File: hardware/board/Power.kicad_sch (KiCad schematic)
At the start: 40 parts

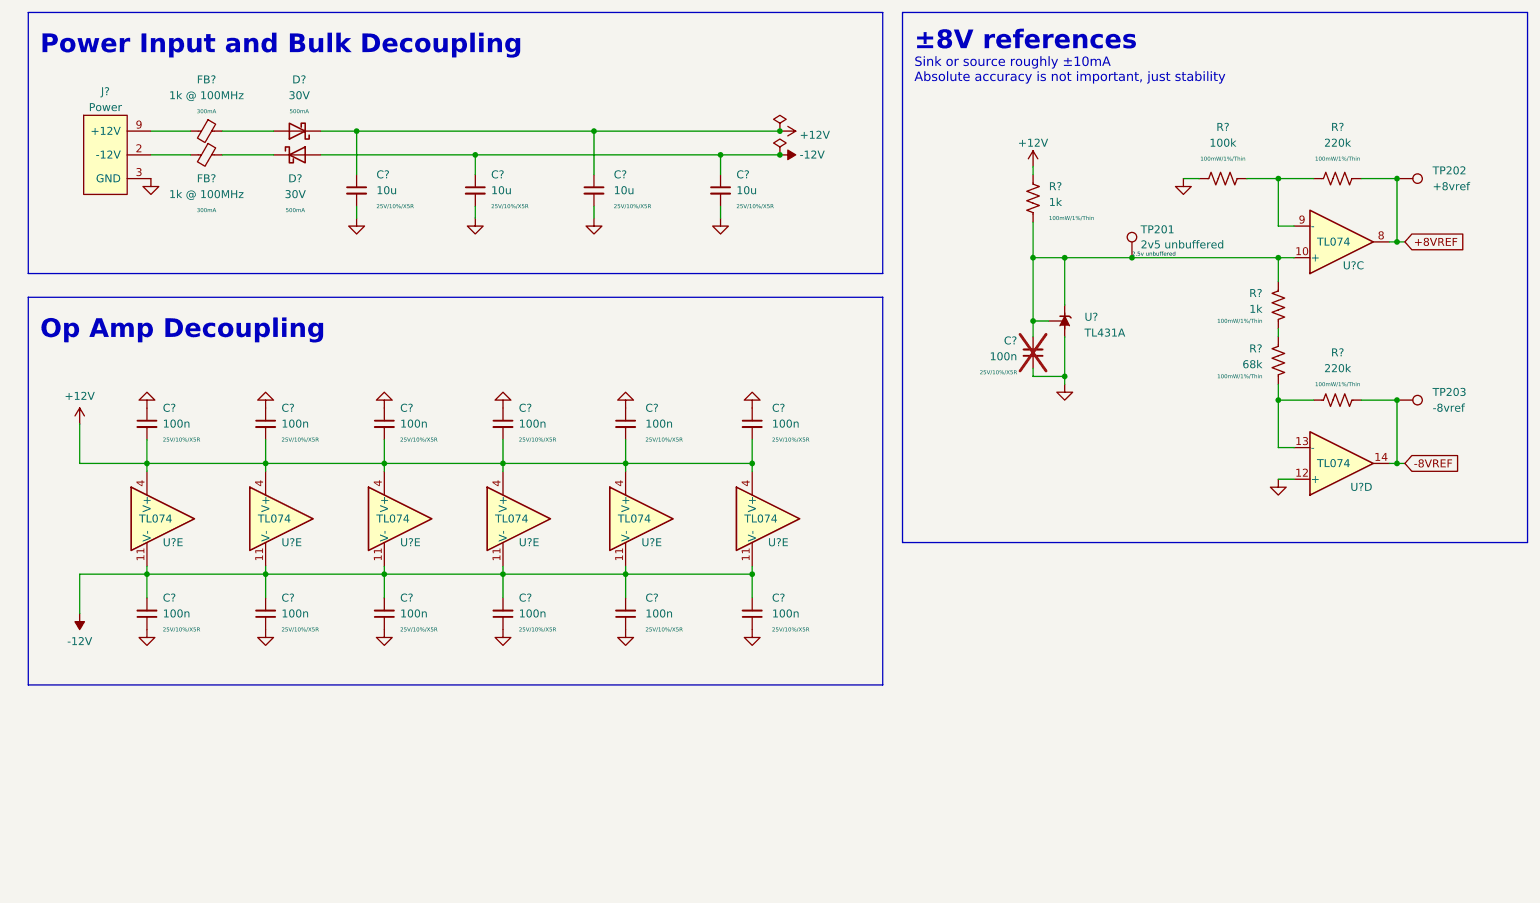
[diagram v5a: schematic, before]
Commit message: hardware: use new Winterbloom sheet layout
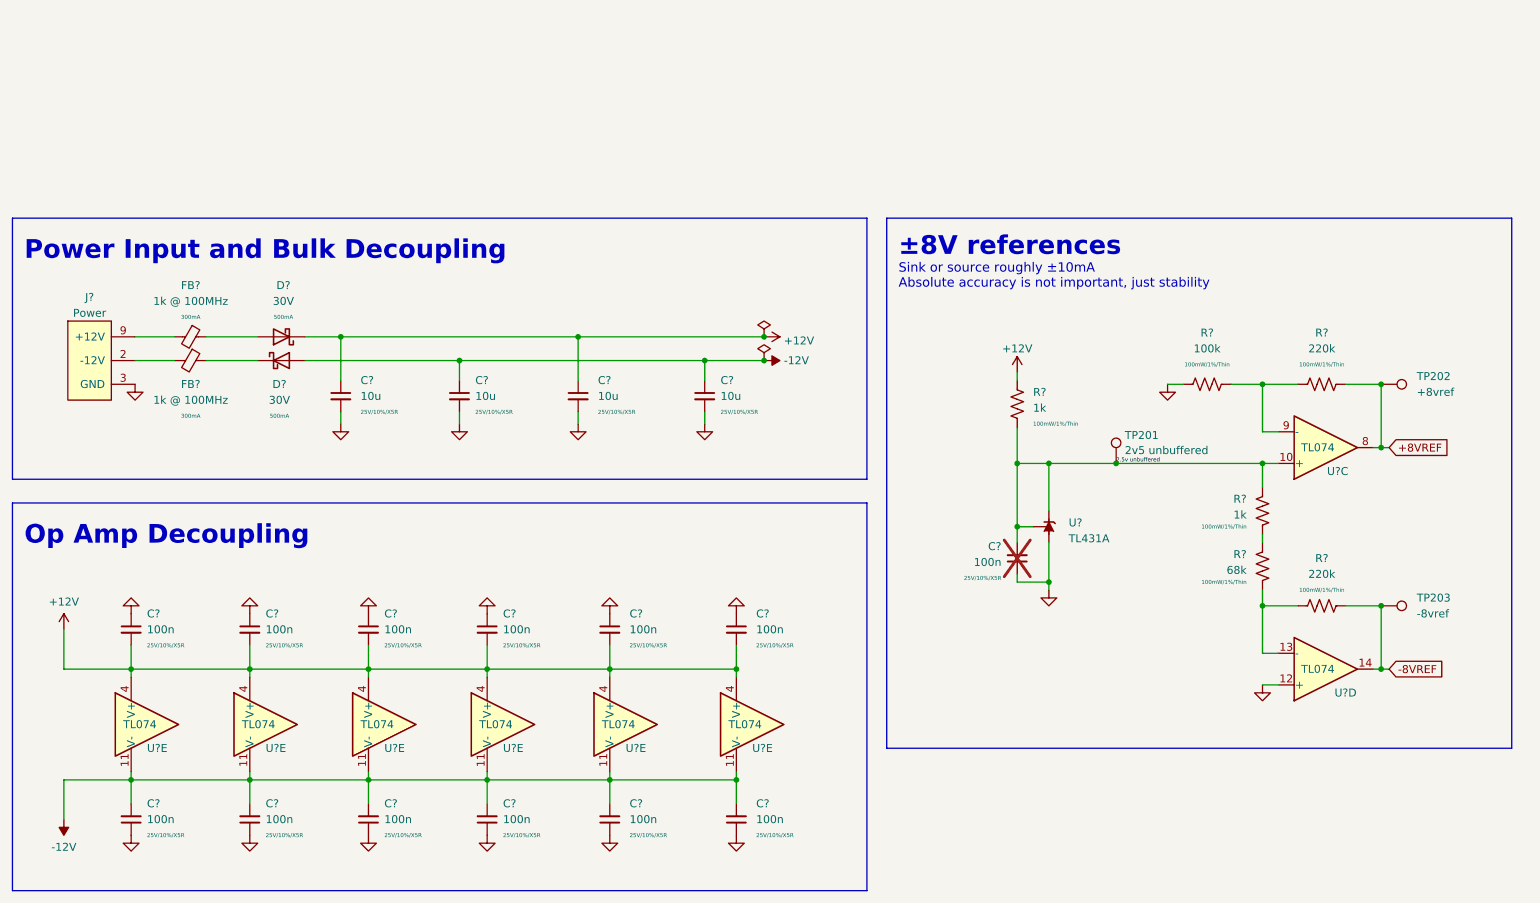
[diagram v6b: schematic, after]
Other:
- moved on the sheet: C?, D?, FB?, J?, R?, TP201, TP202, TP203, U?, U?C, U?D, U?E

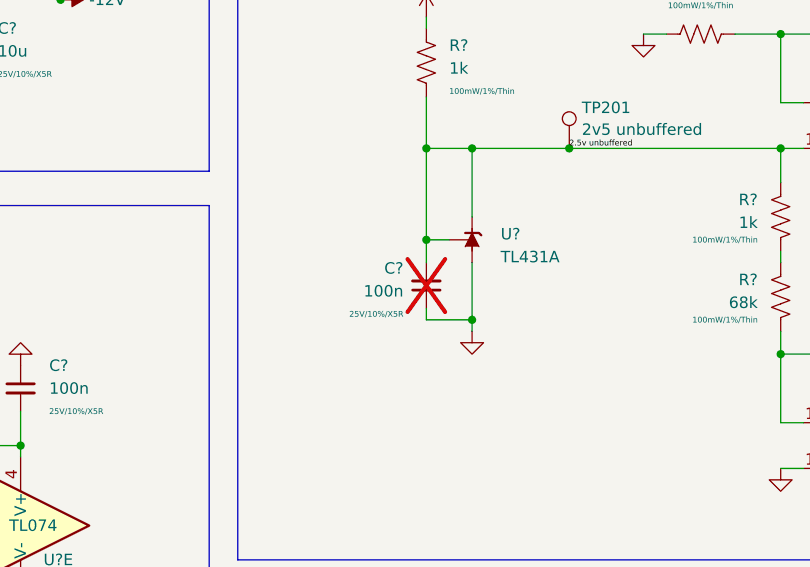
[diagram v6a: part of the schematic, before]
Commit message: Schematic and PCB updates to add offset trim
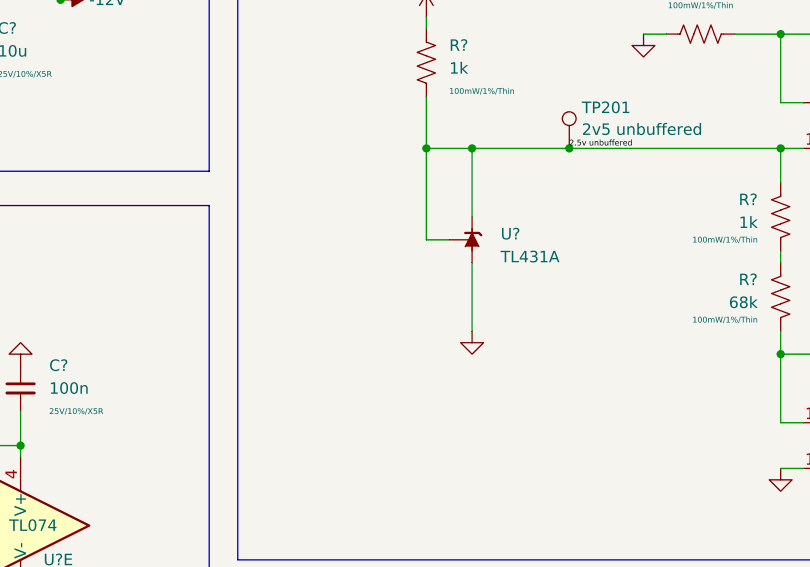
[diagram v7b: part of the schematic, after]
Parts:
- removed C?: 100n, winterbloom:C_0603_HandSolder, symbol Device:C_Small
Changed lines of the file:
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@@
   (junction (at 56.515 126.365) (diameter 0) (color 0 0 0 0)
   )
-  (junction (at 179.705 103.505) (diameter 0) (color 0 0 0 0)
-  )
   (junction (at 114.3 126.365) (diameter 0) (color 0 0 0 0)
   )
@@
   (junction (at 219.075 116.205) (diameter 0) (color 0 0 0 0)
   )
-  (junction (at 184.785 112.395) (diameter 0) (color 0 0 0 0)
-  )
   (junction (at 238.125 116.205) (diameter 0) (color 0 0 0 0)
   )
@@
     (stroke (width 0) (type default))
   )
-  (wire (pts (xy 179.705 103.505) (xy 179.705 106.045))
-    (stroke (width 0) (type default))
-  )
   (wire (pts (xy 221.615 123.825) (xy 219.075 123.825))
     (stroke (width 0) (type default))
@@
     (stroke (width 0) (type default))
   )
-  (wire (pts (xy 179.705 112.395) (xy 179.705 111.125))
-    (stroke (width 0) (type default))
-  )
   (wire (pts (xy 203.835 80.645) (xy 206.375 80.645))
     (stroke (width 0) (type default))
@@
     (stroke (width 0) (type default))
   )
-  (wire (pts (xy 179.705 112.395) (xy 184.785 112.395))
-    (stroke (width 0) (type default))
-  )
   (wire (pts (xy 179.705 93.345) (xy 184.785 93.345))
     (stroke (width 0) (type default))
@@
     (stroke (width 0) (type default))
   )
-  (wire (pts (xy 184.785 106.045) (xy 184.785 112.395))
-    (stroke (width 0) (type default))
-  )
-  (wire (pts (xy 184.785 112.395) (xy 184.785 113.665))
+  (wire (pts (xy 184.785 106.045) (xy 184.785 113.665))
     (stroke (width 0) (type default))
   )
@@
         )
       )
-    )
-  )
-  (symbol (lib_id "Device:C_Small") (at 179.705 108.585 0) (mirror x) (unit 1)
-    (in_bom yes) (on_board yes) (dnp yes)
-    (property "Reference" "C?" (at 177.165 106.6736 0)
-      (effects (font (size 1.27 1.27)) (justify right))
-    )
-    (property "Value" "100n" (at 177.165 109.2136 0)
-      (effects (font (size 1.27 1.27)) (justify right))
-    )
-    (property "Footprint" "winterbloom:C_0603_HandSolder" (at 179.705 108.585 0)
-      (effects (font (size 1.27 1.27)) hide)
-    )
-    (property "Datasheet" "~" (at 179.705 108.585 0)
-      (effects (font (size 1.27 1.27)) hide)
-    )
-    (property "Notes" "Bypass cap" (at 179.705 108.585 0)
-      (effects (font (size 1.27 1.27)) hide)
-    )
-    (property "Rating" "25V/10%/X5R" (at 177.165 111.7536 0)
-      (effects (font (size 0.64 0.64)) (justify right))
-    )
-    (property "MPN" "CL10B104KB8NNNC" (at 179.705 108.585 0)
-      (effects (font (size 1.27 1.27)) hide)
-    )
-    (property "DigiKey" "1276-1000-2-ND" (at 179.705 108.585 0)
-      (effects (font (size 1.27 1.27)) hide)
-    )
-    (property "LCSC" "C1591" (at 179.705 108.585 0)
-      (effects (font (size 1.27 1.27)) hide)
-    )
-    (property "Substitutes Allowed" "Yes" (at 179.705 108.585 0)
-      (effects (font (size 1.27 1.27)) hide)
-    )
-    (pin "1")
-    (pin "2")
-    (instances
-      (project "board"
-        (path "/55082cc1-c956-45a6-b2b5-3db02a6da9d0"
-          (reference "C?") (unit 1)
-        )
-      )
-      (project "mainboard"
-        (path "/960bd036-bf0c-45ea-9f41-1321756e0e5a/2fb572ad-24ea-4cbe-ad52-b6fc76c2d017"
-          (reference "C205") (unit 1)
-        )
-      )
-      (project "VCA"
-        (path "/de69ad6f-07bb-4f9c-962b-520f6532317d"
-          (reference "C?") (unit 1)
-        )
-        (path "/de69ad6f-07bb-4f9c-962b-520f6532317d/0f818280-e6cd-4382-a215-72bb59f50cc3"
-          (reference "C?") (unit 1)
-        )
-      )

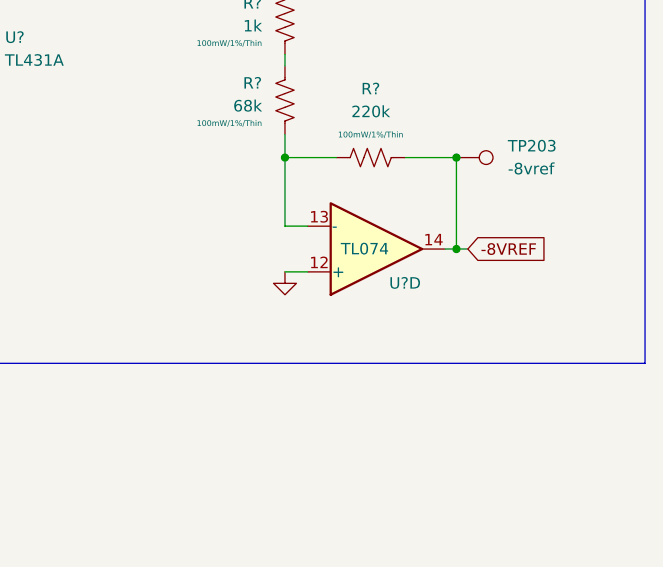
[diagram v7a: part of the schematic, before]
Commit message: hardware: finalize v3
- Updated version number and release date
- Swapped TL074C to TL074H
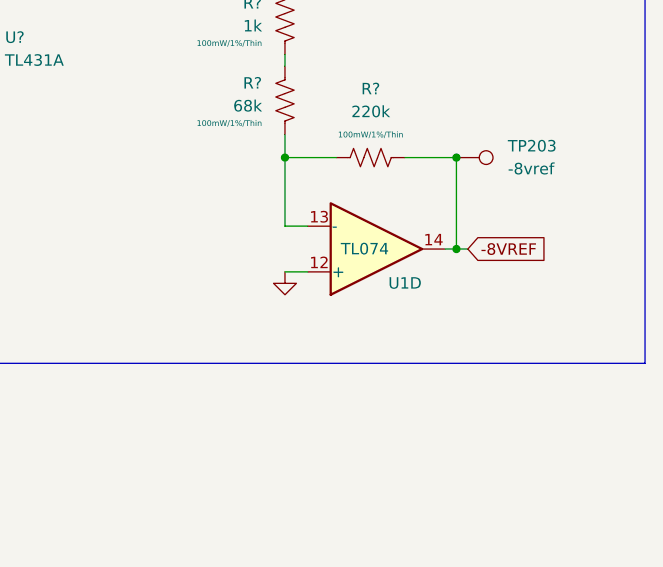
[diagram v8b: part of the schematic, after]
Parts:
- U1: renamed from U?; DigiKey 296-7198-1-ND -> 296-TL074HIPWRCT-ND; LCSC C96507 -> C4370424; MPN TL074CPWR -> TL074HIPWR; Notes (none) -> TL074H over TL074C due to better input offset voltage
- U? (x7): DigiKey 296-7198-1-ND -> 296-TL074HIPWRCT-ND; LCSC C96507 -> C4370424; MPN TL074CPWR -> TL074HIPWR; Notes (none) -> TL074H over TL074C due to better input offset voltage
